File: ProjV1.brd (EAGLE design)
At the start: 77.1 x 41.7 mm, 24 parts, among them IC1 CD4007UBM, IC2 CD4007UBM, IC3 CD4007UBM, U1 MIC5504-3.3YM5-T5, U2 MCP2200-I/SS, U3 ATMEGA328PB-AU, U4 EN11-HSM1BF20, Y1 12MHz

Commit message: Updated Cam Files
Made sure cam files were up to date
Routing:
- net 0: track 0.00 -> 13.1 mm, vias 24 -> 25

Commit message: Updated Cam Files and PDF
Made sure cam files and pdf were up to date
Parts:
- moved T4 0.90 mm to (50.8, 51.5)
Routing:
- net VSET: track 39.9 -> 40.8 mm
- net N$9: track 5.45 -> 4.63 mm
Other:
- board size 77.1 x 41.7 mm -> 77.1 x 42.5 mm
- board text added: "11/10/20 Version 2"
- board text added: "Marcel Vieira"
- board text added: "Pattern Generator"
- board text added: "https://github.com/mvieira4/ECE-388-Pattern-Gerator-Git"

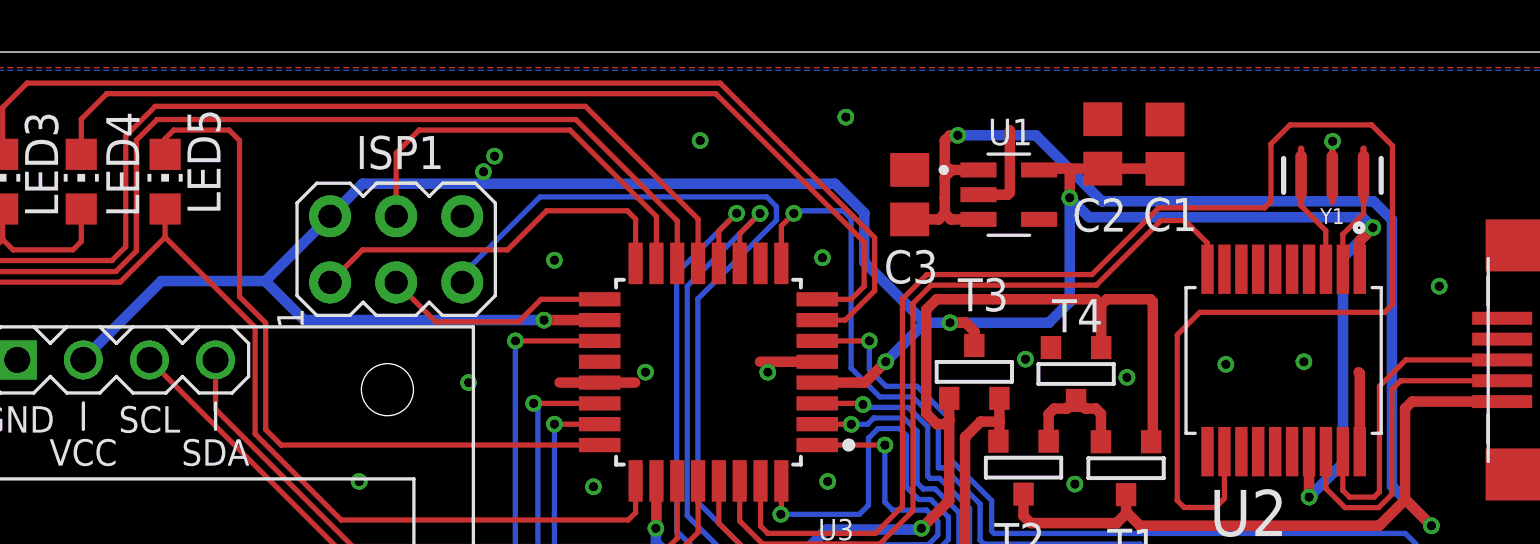
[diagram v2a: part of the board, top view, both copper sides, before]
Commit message: Updated Schematic
Added power flags has issues with flag at output of the  voltage regulator
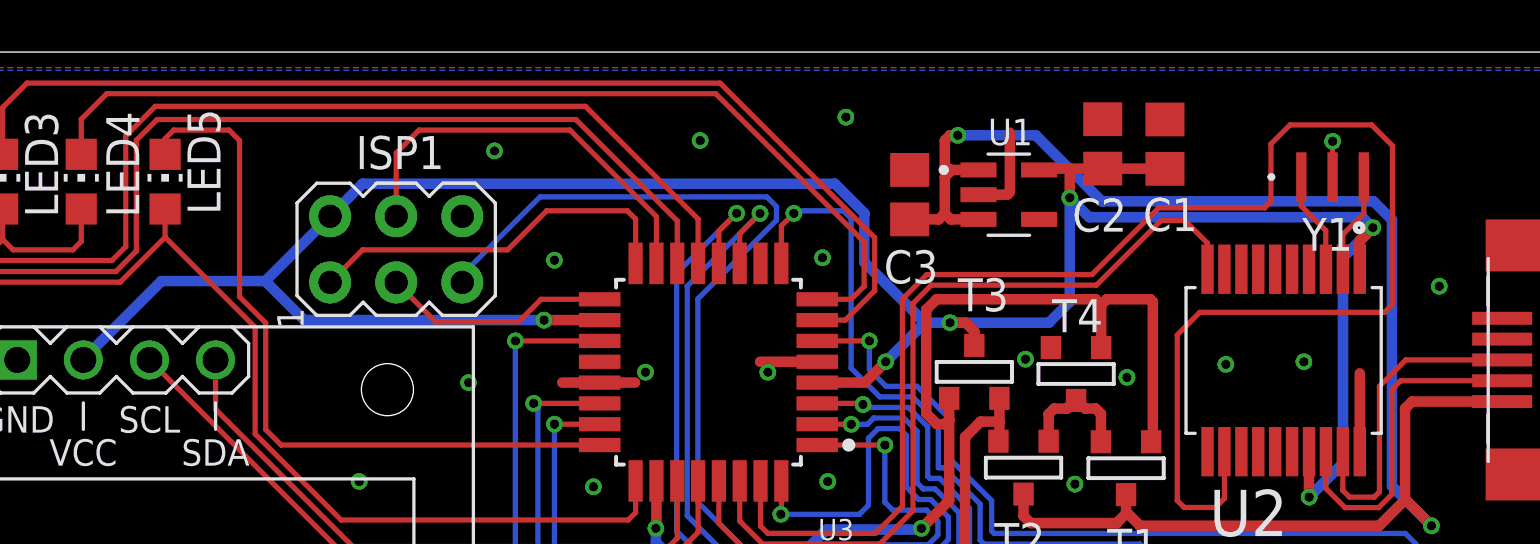
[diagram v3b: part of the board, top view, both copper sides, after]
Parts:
- Y1: value 12MHz -> CSTNE12M0G55A000R0; device SparkFun-Clocks:RESONATOR-SMD-3.2X1.3 -> CSTNE12M0G55A000R0:CSTNE12M0G55A000R0
- moved Y1 0.07 mm to (60.7, 59.1)
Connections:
- net 3.3V renamed +3V3
- net N$14: now also Y1.1; no longer Y1.3
- net N$6: now also Y1.3; no longer Y1.1
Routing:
- net 0: track 13.1 -> 12.8 mm, vias 25 -> 24
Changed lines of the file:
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@@
 <drawing>
 <settings>
-<setting alwaysvectorfont="yes"/>
+<setting alwaysvectorfont="no"/>
 <setting verticaltext="up"/>
 </settings>
 <grid distance="0.1" unitdist="mm" unit="inch" style="lines" multiple="1" display="no" altdistance="5" altunitdist="mil" altunit="mil"/>
 <layers>
-<layer number="1" name="Top" color="4" fill="1" visible="no" active="yes"/>
-<layer number="16" name="Bottom" color="1" fill="1" visible="no" active="yes"/>
+<layer number="1" name="Top" color="4" fill="1" visible="yes" active="yes"/>
+<layer number="16" name="Bottom" color="1" fill="1" visible="yes" active="yes"/>
 <layer number="17" name="Pads" color="2" fill="1" visible="yes" active="yes"/>
 <layer number="18" name="Vias" color="2" fill="1" visible="yes" active="yes"/>
@@
 <attribute name="VENDOR" value="TT Electronics" x="90.17" y="15.24" size="1.778" layer="27" display="off"/>
 </element>
-<element name="Y1" library="SparkFun-Clocks" package="RESONATOR-SMD-3.2X1.3" value="12MHz" x="60.69" y="59.17" smashed="yes" rot="R180">
-<attribute name="NAME" x="60.69" y="57.9" size="0.6096" layer="25" font="vector" ratio="20" rot="R180" align="bottom-center"/>
-<attribute name="PROD_ID" value="XTAL-08900" x="11.16" y="134.1" size="1.778" layer="27" rot="R180" display="off"/>
-<attribute name="VALUE" x="60.69" y="60.44" size="0.6096" layer="27" font="vector" ratio="20" rot="R180" align="top-center"/>
+<element name="Y1" library="CSTNE12M0G55A000R0" package="CSTNE12M0G55A000R0" value="CSTNE12M0G55A000R0" x="60.7" y="59.1" smashed="yes" rot="R180">
+<attribute name="ARROW_PART_NUMBER" value="CSTNE12M0G55A000R0" x="60.7" y="59.1" size="1.778" layer="27" rot="R180" display="off"/>
+<attribute name="ARROW_PRICE-STOCK" value="https://www.arrow.com/en/products/cstne12m0g55a000r0/murata-manufacturing" x="60.7" y="59.1" size="1.778" layer="27" rot="R180" display="off"/>
+<attribute name="DESCRIPTION" value="Resonators 12.0000MHz 33pF SMD CHP Resntr AUTO GRD" x="60.7" y="59.1" size="1.778" layer="27" rot="R180" display="off"/>
+<attribute name="HEIGHT" value="0.8mm" x="60.7" y="59.1" size="1.778" layer="27" rot="R180" display="off"/>
+<attribute name="MANUFACTURER_NAME" value="Murata Electronics" x="60.7" y="59.1" size="1.778" layer="27" rot="R180" display="off"/>
+<attribute name="MANUFACTURER_PART_NUMBER" value="CSTNE12M0G55A000R0" x="60.7" y="59.1" size="1.778" layer="27" rot="R180" display="off"/>
+<attribute name="MOUSER_PART_NUMBER" value="81-CSTNE12M0G55A000R" x="60.7" y="59.1" size="1.778" layer="27" rot="R180" display="off"/>
+<attribute name="MOUSER_PRICE-STOCK" value="https://www.mouser.com/Search/Refine.aspx?Keyword=81-CSTNE12M0G55A000R" x="60.7" y="59.1" size="1.778" layer="27" rot="R180" display="off"/>
+<attribute name="NAME" x="60.5" y="56.9" size="1.27" layer="25" rot="R180" align="center"/>
+<attribute name="VALUE" x="60.3" y="59.1" size="1.27" layer="27" rot="R180" align="center"/>
 </element>
 </elements>
@@
 </signal>
 <signal name="N$14">
-<contactref element="Y1" pad="3"/>
 <contactref element="U2" pad="3"/>
-<wire x1="59.49" y1="59.17" x2="59.49" y2="57.99" width="0.2032" layer="1"/>
 <wire x1="60.4398" y1="57.0402" x2="60.4398" y2="55.5602" width="0.2032" layer="1"/>
 <wire x1="60.4398" y1="55.5602" x2="60.445" y2="55.555" width="0.2032" layer="1"/>
 <wire x1="59.49" y1="57.99" x2="60.4398" y2="57.0402" width="0.2032" layer="1"/>
+<contactref element="Y1" pad="1"/>
+<wire x1="59.5" y1="59.1" x2="59.5" y2="58" width="0.2032" layer="1"/>
+<wire x1="59.5" y1="58" x2="59.49" y2="57.99" width="0.2032" layer="1"/>
 </signal>
 <signal name="0" airwireshidden="yes">
@@
 <contactref element="T4" pad="2"/>
 <contactref element="C3" pad="2"/>
-<contactref element="Y1" pad="2"/>
 <contactref element="IC1" pad="4"/>
 <contactref element="IC1" pad="7"/>
@@
 <vertex x="75.3" y="63.3"/>
 </polygon>
-<via x="28.5" y="59.9" extent="1-16" drill="0.35" grouprefs="0"/>
-<via x="28.0726" y="59.3" extent="1-16" drill="0.35"/>
+<via x="28.5" y="60.1" extent="1-16" drill="0.35" grouprefs="0"/>
 <via x="36.4" y="60.5" extent="1-16" drill="0.35"/>
 <via x="42" y="61.4" extent="1-16" drill="0.35"/>
@@
 <via x="30.8" y="55.9" extent="1-16" drill="0.35"/>
 <contactref element="U2" pad="20"/>
-<wire x1="32.54" y1="51.2" x2="31" y2="51.2" width="0.4064" layer="1"/>
+<wire x1="32.54" y1="51.2" x2="31.1" y2="51.2" width="0.4064" layer="1"/>
 <wire x1="40.9" y1="52" x2="38.7" y2="52" width="0.4064" layer="1"/>
 <wire x1="32.54" y1="51.2" x2="33.9" y2="51.2" width="0.4064" layer="1"/>
 <wire x1="61.745" y1="48.545" x2="61.745" y2="51.555" width="0.4064" layer="1"/>
-<wire x1="61.745" y1="51.555" x2="61.7" y2="51.6" width="0.4064" layer="1"/>
 <wire x1="47.095" y1="58.42" x2="48.22" y2="58.42" width="0.4064" layer="1"/>
-<wire x1="48.22" y1="58.42" x2="48.3" y2="58.5" width="0.4064" layer="1"/>
-<wire x1="48.3" y1="58.5" x2="48.3" y2="60.9" width="0.4064" layer="1"/>
-<wire x1="60.69" y1="59.17" x2="60.69" y2="60.4578" width="0.2032" layer="1"/>
-<wire x1="60.69" y1="60.4578" x2="60.7" y2="60.4678" width="0.2032" layer="1"/>
+<wire x1="48.3" y1="58.5" x2="48.3" y2="60.8" width="0.4064" layer="1"/>
+<contactref element="Y1" pad="2"/>
+<wire x1="60.7" y1="60.4678" x2="60.7" y2="59.1" width="0.2032" layer="1"/>
 <via x="60.7" y="60.4678" extent="1-16" drill="0.35"/>
 </signal>
@@
 </signal>
 <signal name="N$6">
-<contactref element="Y1" pad="1"/>
 <contactref element="U2" pad="2"/>
 <wire x1="61.095" y1="55.555" x2="61.095" y2="56.895" width="0.2032" layer="1"/>
-<wire x1="61.89" y1="57.69" x2="61.89" y2="59.17" width="0.2032" layer="1"/>
-<wire x1="61.89" y1="57.69" x2="61.095" y2="56.895" width="0.2032" layer="1"/>
+<contactref element="Y1" pad="3"/>
+<wire x1="61.9" y1="57.7" x2="61.9" y2="59.1" width="0.2032" layer="1"/>
+<wire x1="61.095" y1="56.895" x2="61.9" y2="57.7" width="0.2032" layer="1"/>
 </signal>
 <signal name="N$30">
@@
 <wire x1="47.095" y1="59.37" x2="46.07" y2="59.37" width="0.4064" layer="1"/>
 <wire x1="46.07" y1="59.37" x2="45.8" y2="59.1" width="0.4064" layer="1"/>
-<wire x1="45.8" y1="57.7" x2="45.8" y2="58.3" width="0.4064" layer="1"/>
-<wire x1="45.8" y1="58.3" x2="45.8" y2="59.1" width="0.4064" layer="1"/>
+<wire x1="45.8" y1="57.7" x2="45.8" y2="59.1" width="0.4064" layer="1"/>
 <wire x1="46.03" y1="57.47" x2="47.095" y2="57.47" width="0.4064" layer="1"/>
 <wire x1="45.8" y1="57.7" x2="46.03" y2="57.47" width="0.4064" layer="1"/>
@@
 <via x="41.1" y="56" extent="1-16" drill="0.35"/>
 </signal>
-<signal name="3.3V">
+<signal name="+3V3">
+<contactref element="T3" pad="1"/>
 <contactref element="ISP1" pad="2"/>
-<contactref element="U1" pad="5"/>
-<contactref element="C2" pad="1"/>
-<contactref element="U3" pad="18"/>
-<contactref element="U3" pad="4"/>
 <contactref element="U2" pad="1"/>
 <contactref element="U2" pad="17"/>
@@
 <wire x1="42.708" y1="55.8242" x2="42.708" y2="57.710425" width="0.4064" layer="16"/>
 <wire x1="42.708" y1="57.710425" x2="41.578225" y2="58.8402" width="0.4064" layer="16"/>
-<wire x1="54.25" y1="59.42" x2="54.26" y2="59.41" width="0.4064" layer="1"/>
+<wire x1="19.69" y1="55.1" x2="15.7" y2="55.1" width="0.4064" layer="16"/>
+<via x="30.4" y="53.6" extent="1-16" drill="0.35"/>
+<wire x1="21.19" y1="53.6" x2="30.4" y2="53.6" width="0.4064" layer="16"/>
+<wire x1="41.578225" y1="58.8402" x2="23.4302" y2="58.8402" width="0.4064" layer="16"/>
+<wire x1="50.6" y1="58.3" x2="50.6" y2="59.42" width="0.4064" layer="1"/>
+<wire x1="46.6" y1="53.5" x2="46.9346" y2="53.1654" width="0.4064" layer="1"/>
+<wire x1="21.19" y1="53.6" x2="19.69" y2="55.1" width="0.4064" layer="16"/>
+<contactref element="C2" pad="1"/>
+<contactref element="U3" pad="18"/>
+<contactref element="U3" pad="4"/>
 <contactref element="U$1" pad="2"/>
-<wire x1="15.7" y1="55.1" x2="19.69" y2="55.1" width="0.4064" layer="16"/>
 <wire x1="15.7" y1="55.1" x2="12.7" y2="52.1" width="0.4064" layer="16"/>
 <wire x1="12.7" y1="52.1" x2="12.7" y2="52.07" width="0.4064" layer="16"/>
-<via x="30.4" y="53.6" extent="1-16" drill="0.35"/>
-<wire x1="21.19" y1="53.6" x2="30.4" y2="53.6" width="0.4064" layer="16"/>
-<wire x1="40.9" y1="51.2" x2="42.7322" y2="51.2" width="0.4064" layer="1"/>
 <wire x1="32.54" y1="53.6" x2="30.4" y2="53.6" width="0.4064" layer="1"/>
-<wire x1="23.4302" y1="58.8402" x2="22.18" y2="57.59" width="0.4064" layer="16"/>
-<wire x1="41.578225" y1="58.8402" x2="23.4302" y2="58.8402" width="0.4064" layer="16"/>
+<wire x1="42.7322" y1="51.2" x2="40.9" y2="51.2" width="0.4064" layer="1"/>
+<wire x1="51.87" y1="59.42" x2="50.6" y2="59.42" width="0.4064" layer="1"/>
+<wire x1="51.87" y1="59.42" x2="54.25" y2="59.42" width="0.4064" layer="1"/>
+<wire x1="54.25" y1="59.42" x2="54.26" y2="59.41" width="0.4064" layer="1"/>
+<contactref element="U1" pad="5"/>
 <wire x1="49.425" y1="59.37" x2="49.475" y2="59.42" width="0.4064" layer="1"/>
 <wire x1="49.475" y1="59.42" x2="50.6" y2="59.42" width="0.4064" layer="1"/>
-<wire x1="50.6" y1="59.42" x2="51.87" y2="59.42" width="0.4064" layer="1"/>
-<wire x1="50.6" y1="58.3" x2="50.6" y2="59.42" width="0.4064" layer="1"/>
-<wire x1="51.87" y1="59.42" x2="54.25" y2="59.42" width="0.4064" layer="1"/>
-<contactref element="T3" pad="1"/>
-<wire x1="46.6" y1="53.5" x2="46.9346" y2="53.1654" width="0.4064" layer="1"/>
+<wire x1="23.4302" y1="58.8402" x2="22.18" y2="57.59" width="0.4064" layer="16"/>
+<wire x1="19.69" y1="55.1" x2="22.18" y2="57.59" width="0.4064" layer="16"/>
 <wire x1="46.9346" y1="53.1654" x2="46.9346" y2="52.626" width="0.4064" layer="1"/>
-<wire x1="22.18" y1="57.59" x2="19.69" y2="55.1" width="0.4064" layer="16"/>
-<wire x1="19.69" y1="55.1" x2="21.19" y2="53.6" width="0.4064" layer="16"/>
 </signal>
 </signals>

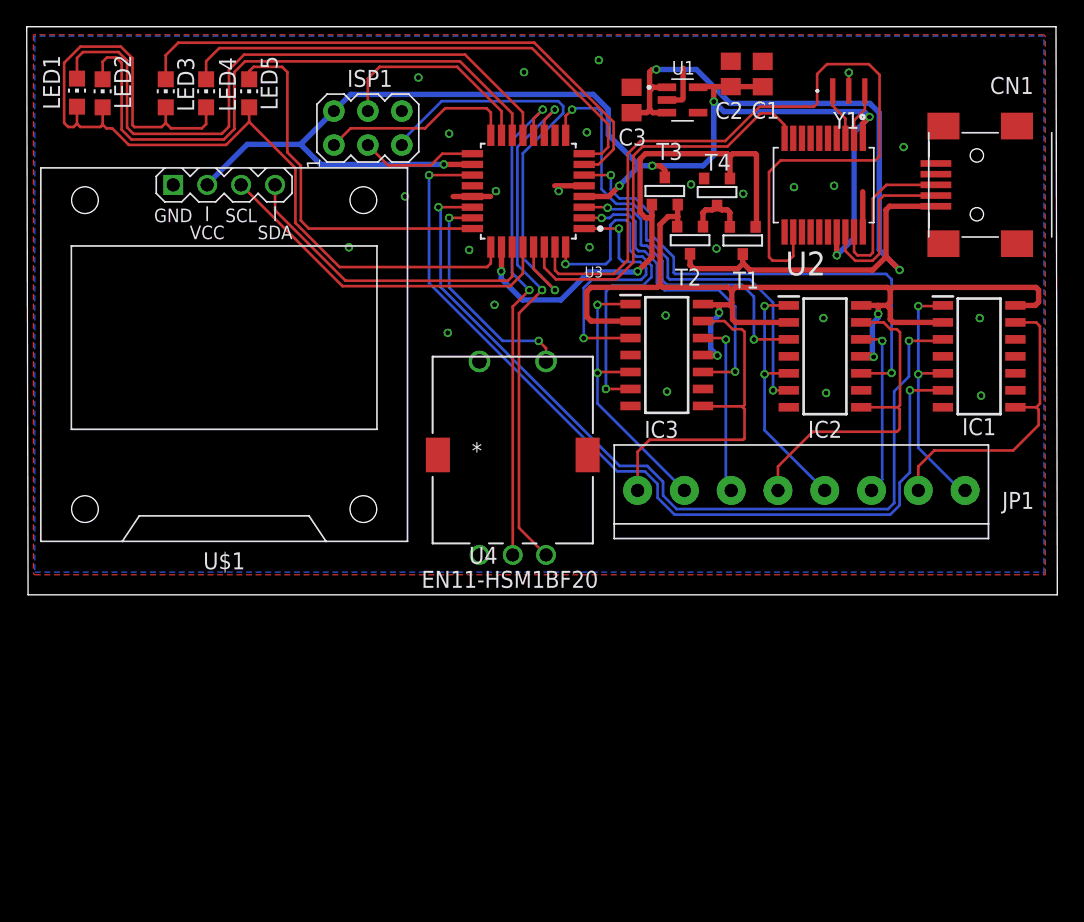
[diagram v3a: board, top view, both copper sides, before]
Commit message: Updated Schematic
Fixed usb, made power source changes, got rid of missing part error relayed out board
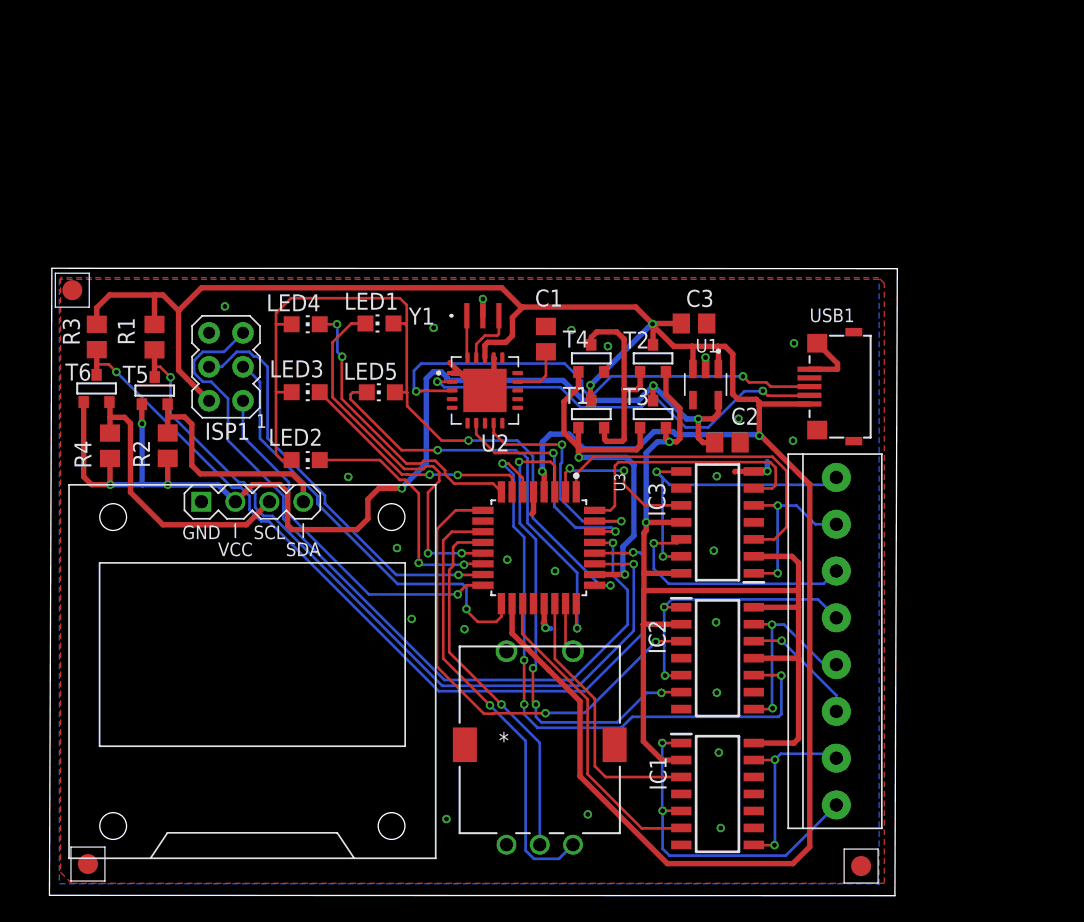
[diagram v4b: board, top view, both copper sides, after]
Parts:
- removed CN1: (no value), adafruit:USB-MINIB
- added R1, R2, R3, R4: 10k, rcl:R0805
- added T5, T6: (no value), zetex:SOT-23
- added U$2, U$3, U$4: (no value), dicons:FIDUCIAL_G15S
- added USB1: C77238, usbFromLCSC:C77238
- U2: value MCP2200-I/SS -> MCP2200-I/MQ; device MCP2200-I_SS:SOP65P780X200-20N -> MCP2200-I_MQ:QFN65P500X500X100-21N
- moved IC1 38.1 mm to (50.9, 6.50)
- moved Y1 32.1 mm to (33.3, 42.3)
- moved LED2 31.4 mm to (20.1, 31.5), turned to 270 degrees
- moved U2 29.6 mm to (33.5, 36.7), turned to 0 degrees
- moved LED1 28.5 mm to (25.6, 41.7), turned to 90 degrees
- moved C2 27.6 mm to (51.6, 32.8), turned to 0 degrees
- moved U3 26.7 mm to (37.5, 24.9), turned to 270 degrees
- moved C1 25.6 mm to (38.0, 40.5)
- moved LED3 24.7 mm to (20.1, 36.6), turned to 270 degrees
- moved LED5 24.4 mm to (25.7, 36.5), turned to 90 degrees
- moved IC2 24.0 mm to (50.9, 16.7)
- moved U$1 23.8 mm to (16.1, 15.7)
- moved U4 21.8 mm to (37.6, -5.17)
- moved U1 21.4 mm to (50.0, 37.1), turned to 270 degrees
- moved ISP1 20.8 mm to (14.1, 38.5), turned to 180 degrees
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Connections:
- removed net N$8: CN1.ID
- removed net RX/TX: U2.10, U3.30
- removed net TX/RX: U2.12, U3.31
- new net N$10: U2.7, U3.30
- new net N$11: U2.9, U3.31
- new net N$16: R2.1, T5.2, U$1.4
- new net N$19: R4.1, T6.2, U$1.3
- new net N$7: C1.1, U2.14
- net +3V3: now also R2.2, R4.2, T5.3, T6.3; no longer C1.1, ISP1.2, U2.1, U2.17, U3.18, U3.4
- net +5V: now also ISP1.2, R1.2, R3.2, U2.18, U3.18, U3.4, USB1.1; no longer CN1.VBUS
- net 0: now also U2.1, U2.17, U2.21, USB1.0, USB1.0A, USB1.0B, USB1.0C, USB1.5; no longer CN1.GND, U2.20
- net C4: now also IC2.1, IC2.5; no longer IC2.13, IC2.8
- net C5: now also IC2.13, IC2.8; no longer IC2.1, IC2.5
- net D+: now also U2.3, USB1.3; no longer CN1.D+, U2.19
- net D-: now also U2.2, USB1.2; no longer CN1.D-, U2.18
- net LC4: now also IC2.3; no longer IC2.6
- net LC5: now also IC2.6; no longer IC2.3
- net N$14: now also U2.20; no longer U2.3
- net N$6: now also U2.19; no longer U2.2
- net SCL: now also R3.1, T6.1; no longer U$1.3
- net SDA: now also R1.1, T5.1; no longer U$1.4
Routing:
- net +5V: track 63.8 -> 183.8 mm, vias 2 -> 4
- net TX/RX: track 64.0 -> 0.00 mm
- net LC8: track 65.4 -> 20.2 mm, vias 2 -> 0
- net LC7: track 66.0 -> 23.5 mm, vias 2 -> 0
- net SCL: track 26.6 -> 64.9 mm, vias 0 -> 2
- net SDA: track 24.2 -> 59.6 mm, vias 0 -> 2
- net RX/TX: track 31.1 -> 0.00 mm
- net LED2: track 45.7 -> 18.6 mm, vias 0 -> 2
- net RST: track 34.1 -> 59.9 mm
- net LED3: track 42.9 -> 18.1 mm, vias 0 -> 2
- net D+: track 12.3 -> 36.3 mm, vias 0 -> 2
- net SCK: track 8.81 -> 32.2 mm, vias 0 -> 1
- net N$19: track 0.00 -> 21.3 mm
- net LED1: track 49.0 -> 28.2 mm, vias 0 -> 2
- net D-: track 12.9 -> 32.1 mm, vias 0 -> 2
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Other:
- board size 77.1 x 42.5 mm -> 63.4 x 46.9 mm
- board text added: "Marcel Vieira 11/12/20 Version 4"
- board text removed: "11/10/20 Version 2"
- board text removed: "Marcel Vieira"
- board text removed: "Pattern Generator"

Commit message: Updated Gerbers
Reuploaded incase of erros
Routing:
- net 0: vias 21 -> 24
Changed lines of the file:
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@@
 <wire x1="39.2364" y1="32.6436" x2="35.0072125" y2="32.6436" width="0.2032" layer="1"/>
-</signal>
-<signal name="N$8">
-<via x="26.9" y="24.9" extent="1-16" drill="0.35"/>
-</signal>
-<signal name="N$23">
-<via x="41.175" y="4.975" extent="1-16" drill="0.35"/>
-</signal>
-<signal name="N$24">
-<via x="30.6" y="4.625" extent="1-16" drill="0.35"/>
 </signal>
 <signal name="0">
@@
 <wire x1="33.48" y1="36.69" x2="32.935" y2="36.69" width="0.4064" layer="1"/>
 <wire x1="32.935" y1="36.69" x2="30.85" y2="38.775" width="0.4064" layer="1"/>
+<via x="41.175" y="4.975" extent="1-16" drill="0.35"/>
+<via x="30.6" y="4.625" extent="1-16" drill="0.35"/>
+<via x="26.9" y="24.9" extent="1-16" drill="0.35"/>
 </signal>
 <signal name="N$15">
